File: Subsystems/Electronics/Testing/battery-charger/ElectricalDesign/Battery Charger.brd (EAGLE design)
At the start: 100 x 80 mm, 61 parts, among them J1 USB4515-GF-A_REVA, Q1 CSD16406Q3, Q2 CSD16406Q3, Q3 DMN2008LFU, Q4 DMN2008LFU, Q5 DMN2008LFU, U1 BQ24650, U2 BQ29700, U3 BQ29700, U4 BQ29700

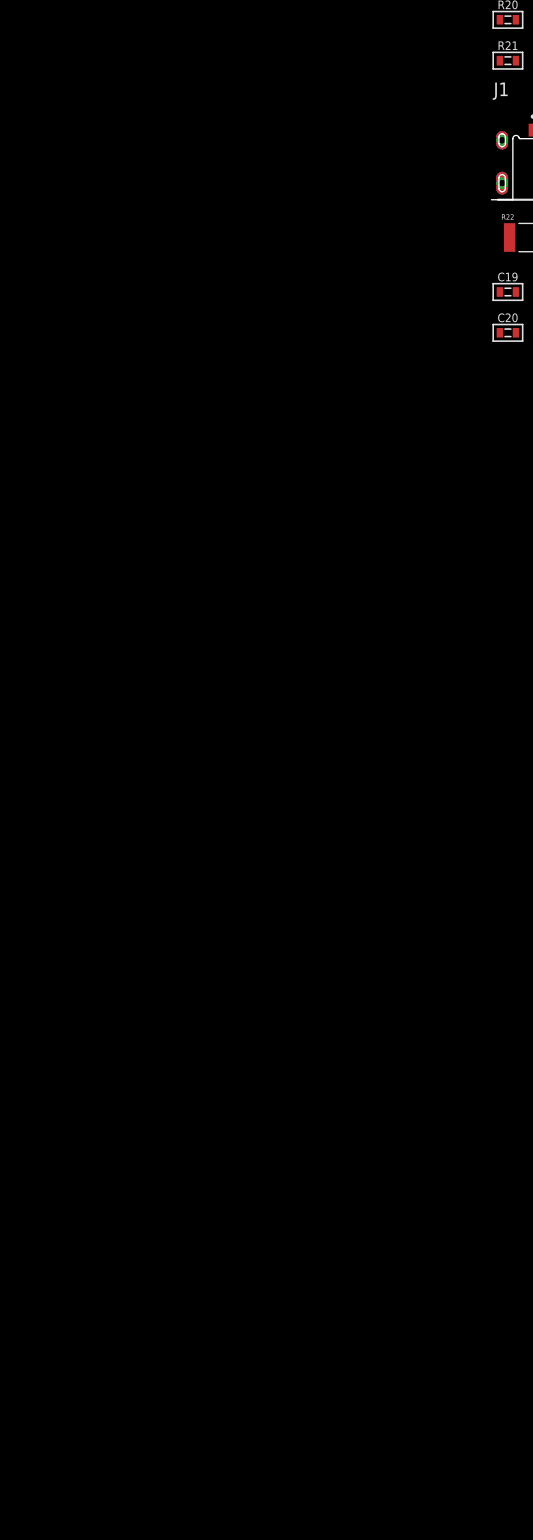
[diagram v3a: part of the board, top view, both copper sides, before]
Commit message: Finished Switching and Battery Protection Circuits
Pages 1-3 are basically finished, while the main components for page 4 have been imported
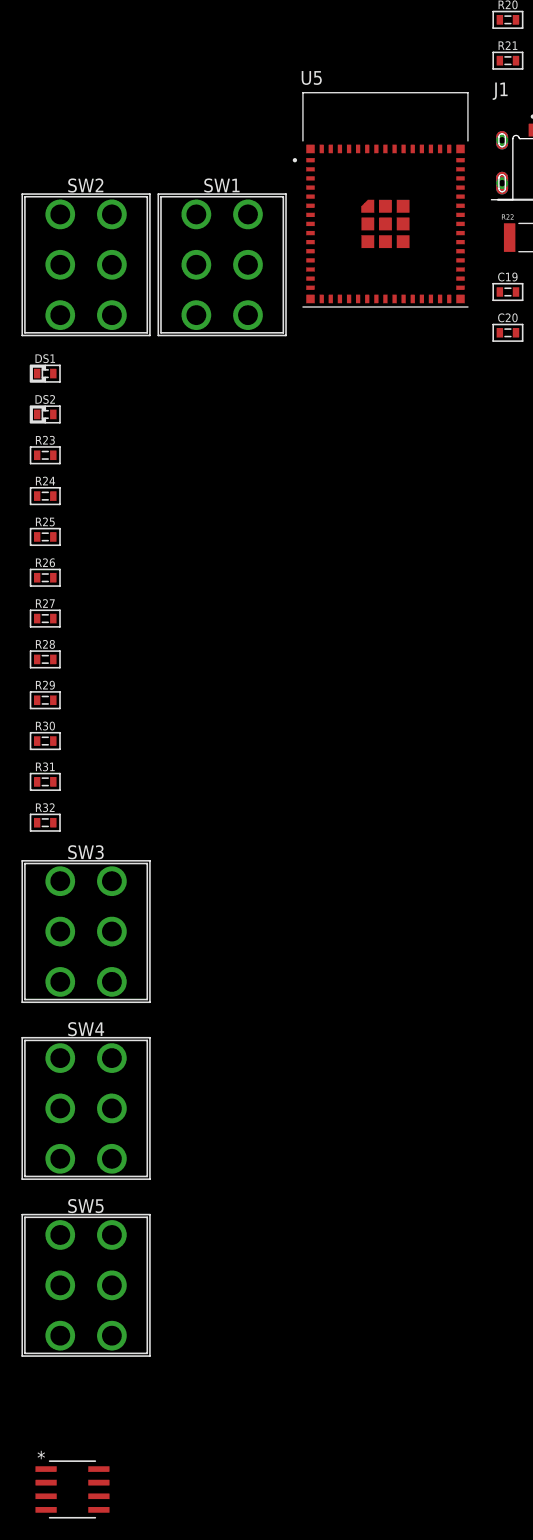
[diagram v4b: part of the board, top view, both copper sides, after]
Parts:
- added DS1: Red, CougsInSpace-LEDs:1608-POL
- added DS2: Green, CougsInSpace-LEDs:1608-POL
- added R23, R24: 10kΩ 0.1%, CougsInSpace-Resistors:1608
- added R25, R28, R30, R32: 442kΩ 1%, CougsInSpace-Resistors:1608
- added R26, R27, R29, R31: 33kΩ 1%, CougsInSpace-Resistors:1608
- added SW1, SW2, SW3, SW4, SW5: (no value), CougsInSpace-Switches:100DP1T1B1M2QE
- added U5: ESP32-S2-MINI-1, ESP32-S2-MINI-1:XCVR_ESP32-S2-MINI-1
- added U7: LT1129IS8-3.3, LT1129IS8-3.3:SO-8_S
- C20: value 1µF 10% -> 10µF 10%
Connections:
- new net 3V3: U5.3
- new net GND: U5.1, U5.2, U5.30, U5.42, U5.43, U5.46, U5.47, U5.48, U5.49, U5.50, U5.51, U5.52, U5.53, U5.54, U5.55, U5.56, U5.57, U5.58, U5.59, U5.60, U5.61, U5.61_1, U5.61_2, U5.61_3, U5.61_4, U5.61_5, U5.61_6, U5.61_7, U5.61_8, U5.62, U5.63, U5.64, U5.65
- new net N$21: U7.1, U7.2
- new net N$33: DS2.A, R24.1
- new net N$34: C19.1, C20.1, R22.1
- new net N$35: R25.1, R26.2
- new net N$36: R27.2, R28.1
- new net N$37: R29.2, R30.1
- new net N$38: R31.2, R32.1
- new net STAT1: D1.4, R26.1
- new net STAT2: DS1.C, U1.3
- new net STAT3: DS2.C, U1.5
- new net STAT4: D3.4, R27.1
- new net STAT5: D4.4, R29.1
- new net STAT6: D5.4, R31.1
- new net SW1: D1.3, SW1.COM-A, SW1.COM-B
- new net SW2: R4.1, R5.2, SW2.COM-A, SW2.COM-B, U1.2
- new net SW3: D3.3, SW3.COM-A, SW3.COM-B
- new net SW4: D4.3, SW4.COM-A, SW4.COM-B
- new net SW5: D5.3, SW5.COM-A, SW5.COM-B
- net 5.0V: now also R23.2, R24.2, R25.2, R28.2, R30.2, R32.2, SW1.1-A, SW1.1-B, SW3.1-A, SW3.1-B, SW4.1-A, SW4.1-B, SW5.1-A, SW5.1-B, U7.8
- net N$11: now also DS1.A, R23.1; no longer R4.1, R5.2, U1.2
- net PGND: now also C19.2, C20.2, SW1.2-A, SW1.2-B, SW2.1-A, SW2.1-B, SW3.2-A, SW3.2-B, SW4.2-A, SW4.2-B, SW5.2-A, SW5.2-B, U7.3, U7.6, U7.7

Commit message: USB to UART IC Added
Page 4 should now be complete with the implementation of a USB to UART program converter. ESP32 has been moved to page 5 and outside of the thermistor connection on the charge controller, this should be the last page
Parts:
- added C25, C26: 4.7µF 10%, CougsInSpace-Capacitors:3216
- added C27, C28, C30, C31: 100nF 10%, CougsInSpace-Capacitors:1608
- added C29: 10µF 10%, CougsInSpace-Capacitors:1608
- added C32: C1206C226K8RACTU, C1206C226K8RACTU:CAPC3216X110N
- added DS3, DS4: Green, CougsInSpace-LEDs:1608-POL
- added J2: (no value), CougsInSpace-Connectors:USB-B-FEMALE
- added Q6, Q7: BC817, BC817:SOT95P230X110-3N
- added R33, R34, R35, R36: 10kΩ 0.1%, CougsInSpace-Resistors:1608
- added U$1: LD1117AS33, LD1117AS33:SOT223
- U5: value ESP32-S2-MINI-1 -> CP2102N-A02-GQFN28; device ESP32-S2-MINI-1:XCVR_ESP32-S2-MINI-1 -> CP2102N-A02-GQFN28:QFN50P500X500X80-29N
- U7: value LT1129IS8-3.3 -> ESP32-S2-MINI-1; device LT1129IS8-3.3:SO-8_S -> ESP32-S2-MINI-1:XCVR_ESP32-S2-MINI-1
- moved U5 221.9 mm to (-133.3, -417.8)
- moved U7 69.5 mm to (-104.1, -395.0)
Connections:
- removed net 3V3: U5.3
- removed net GND: U5.1, U5.2, U5.30, U5.42, U5.43, U5.46, U5.47, U5.48, U5.49, U5.50, U5.51, U5.52, U5.53, U5.54, U5.55, U5.56, U5.57, U5.58, U5.59, U5.60, U5.61, U5.61_1, U5.61_2, U5.61_3, U5.61_4, U5.61_5, U5.61_6, U5.61_7, U5.61_8, U5.62, U5.63, U5.64, U5.65
- new net N$25: J2.3, U5.4
- new net N$31: J2.2, U5.5
- new net N$42: C25.1, C27.1, J2.1, R35.2, R36.2, U5.7, U5.8
- new net N$43: DS4.C, U5.18
- new net N$44: C29.1, C31.1, C32.2, U$1.2, U7.3
- new net N$45: DS3.C, U5.19
- new net N$46: Q6.2, R34.1, U5.24
- new net N$47: Q7.2, R33.1, U5.28
- new net N$48: Q7.1, R34.2
- new net N$49: Q6.1, R33.2
- new net N$50: DS3.A, R35.1
- new net N$51: DS4.A, R36.1
- new net UART-ESP_EN: Q6.3
- new net UART-ESP_IO0: Q7.3
- new net UART_RXD-ESP_TXD: U5.25
- new net UART_TXD-ESP_RXD: U5.26
- net 5.0V: now also C30.1, U$1.3; no longer U7.8
- net N$21: now also C26.1, C28.1, U5.6; no longer U7.1, U7.2
- net PGND: now also C25.2, C26.2, C27.2, C28.2, C29.2, C30.2, C31.2, C32.1, J2.4, J2.SHIELD@1, J2.SHIELD@2, U$1.1, U5.29, U5.3, U7.1, U7.2, U7.30, U7.42, U7.43, U7.46, U7.47, U7.48, U7.49, U7.50, U7.51, U7.52, U7.53, U7.54, U7.55, U7.56, U7.57, U7.58, U7.59, U7.60, U7.61, U7.61_1, U7.61_2, U7.61_3, U7.61_4, U7.61_5, U7.61_6, U7.61_7, U7.61_8, U7.62, U7.63, U7.64, U7.65; no longer U7.3, U7.6, U7.7
- net STAT1: now also U7.5
- net STAT2: now also U7.6
- net STAT3: now also U7.7
- net STAT4: now also U7.8
- net STAT5: now also U7.9
- net STAT6: now also U7.10

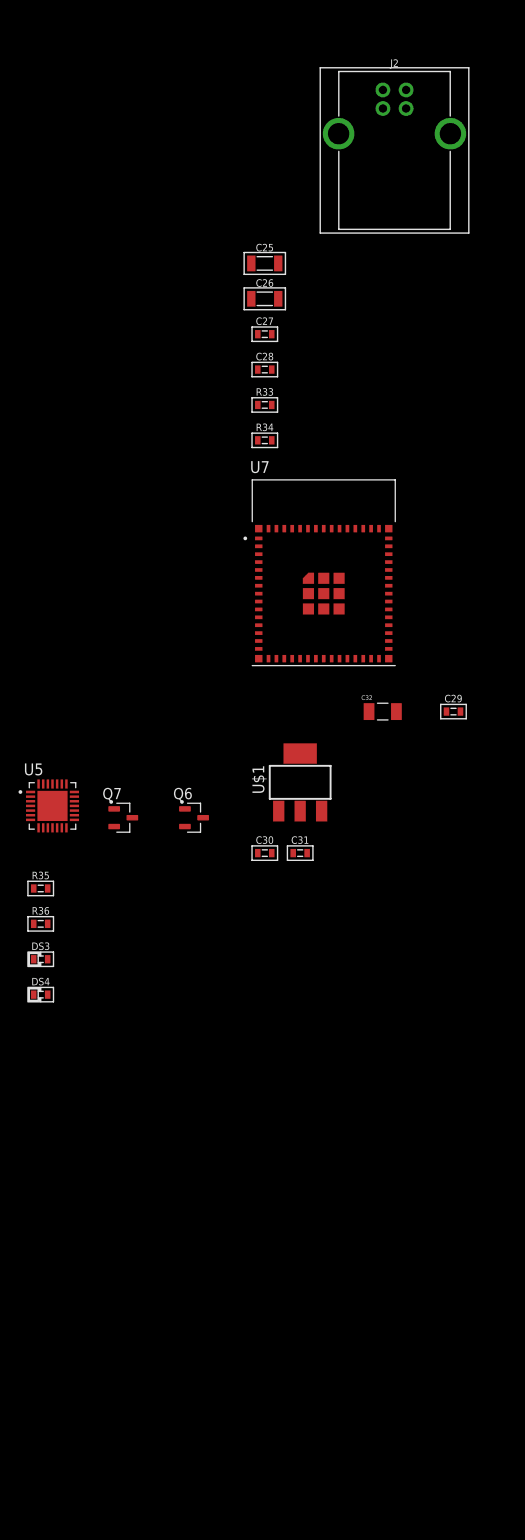
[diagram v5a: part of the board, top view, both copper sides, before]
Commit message: Finished Battery Charger V1
Will add programmable RGB LEDS at some point, and may update at a later date with an LED display, but otherwise this can be considered the base design for the over-engineered battery charger
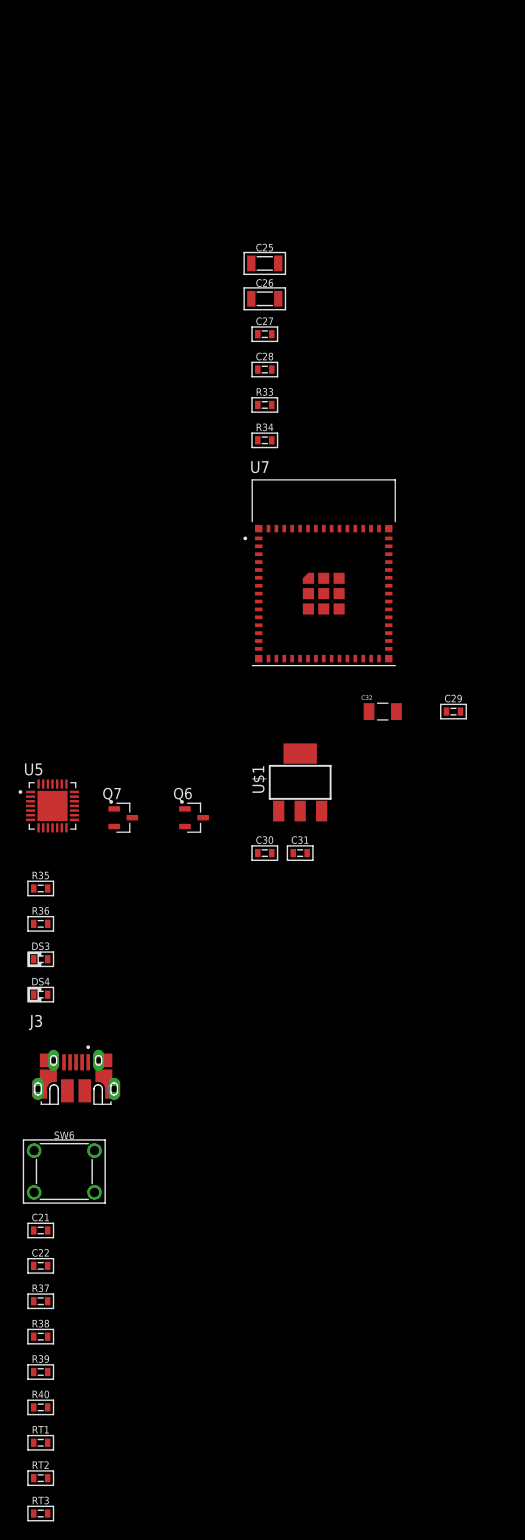
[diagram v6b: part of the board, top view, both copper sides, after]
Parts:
- removed J2: (no value), CougsInSpace-Connectors:USB-B-FEMALE
- added C21, C22: 100nF 10%, CougsInSpace-Capacitors:1608
- added J3: 10103592-0001LF, 10103592-0001LF:AMPHENOL_10103592-0001LF
- added R37, R38, R39, R40: 10kΩ 0.1%, CougsInSpace-Resistors:1608
- added RT1, RT2, RT3: 10kΩ 5%, CougsInSpace-Resistors:1608
- added SW6: [Override], CougsInSpace-Switches:THT-6060
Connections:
- removed net N$44: C29.1, C31.1, C32.2, U$1.2, U7.3
- new net 3.3V: C29.1, C31.1, C32.2, R37.2, R38.2, R39.2, R40.2, U$1.2, U7.3
- new net TEMP1: R38.1, RT1.2, U7.11
- new net TEMP2: R39.1, RT2.2, U7.12
- new net TEMP3: R40.1, RT3.2, U7.13
- new net TS-ESP: U1.4, U7.14
- net N$25: now also J3.3; no longer J2.3
- net N$31: now also J3.2; no longer J2.2
- net N$42: now also J3.1; no longer J2.1
- net PGND: now also C21.1, C22.2, J3.5, J3.S1, J3.S2, J3.S3, J3.S4, J3.S5, J3.S6, RT1.1, RT2.1, RT3.1, SW6.1, SW6.2; no longer J2.4, J2.SHIELD@1, J2.SHIELD@2
- net UART-ESP_EN: now also C21.2, C22.1, R37.1, SW6.3, SW6.4, U7.45
- net UART-ESP_IO0: now also U7.4
- net UART_RXD-ESP_TXD: now also U7.39
- net UART_TXD-ESP_RXD: now also U7.40

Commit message: Added RGB LEDs
Final touches for V1 including CAD notes and addressable LEDs have been added
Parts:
- added C23, C24, C33: 100nF 10%, CougsInSpace-Capacitors:1608
- added D6, D7, D8: SK6812, SK6812:LED_SK6812
- added JP1: (no value), pinhead:1X07
- added JP2: (no value), pinhead:1X16
- added R41: 330Ω 1%, CougsInSpace-Resistors:1608
- DS1: value Red -> Yellow
- moved DS1 277.5 mm to (-134.6, -497.8)
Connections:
- new net LEDS: R41.1, U7.15
- new net N$44: JP2.1, U7.23
- new net N$52: JP2.2, U7.24
- new net N$53: JP2.3, U7.25
- new net N$54: JP2.4, U7.26
- new net N$55: JP2.5, U7.28
- new net N$56: JP2.6, U7.29
- new net N$57: JP2.7, U7.31
- new net N$58: JP2.8, U7.32
- new net N$59: JP2.9, U7.33
- new net N$60: JP2.10, U7.34
- new net N$61: JP2.11, U7.35
- new net N$62: JP2.12, U7.36
- new net N$63: JP2.13, U7.37
- new net N$64: JP2.14, U7.38
- new net N$65: JP2.15, U7.41
- new net N$66: JP2.16, U7.44
- new net N$67: D7.2, D8.4
- new net N$68: JP1.7, U7.16
- new net N$69: JP1.6, U7.17
- new net N$70: JP1.5, U7.18
- new net N$71: JP1.4, U7.19
- new net N$72: JP1.3, U7.20
- new net N$73: JP1.2, U7.21
- new net N$74: JP1.1, U7.22
- new net N$76: D6.2, D7.4
- new net N$77: D6.4, R41.2
- net 5.0V: now also C23.1, C24.1, C33.1, D6.1, D7.1, D8.1
- net PGND: now also C23.2, C24.2, C33.2, D6.3, D7.3, D8.3

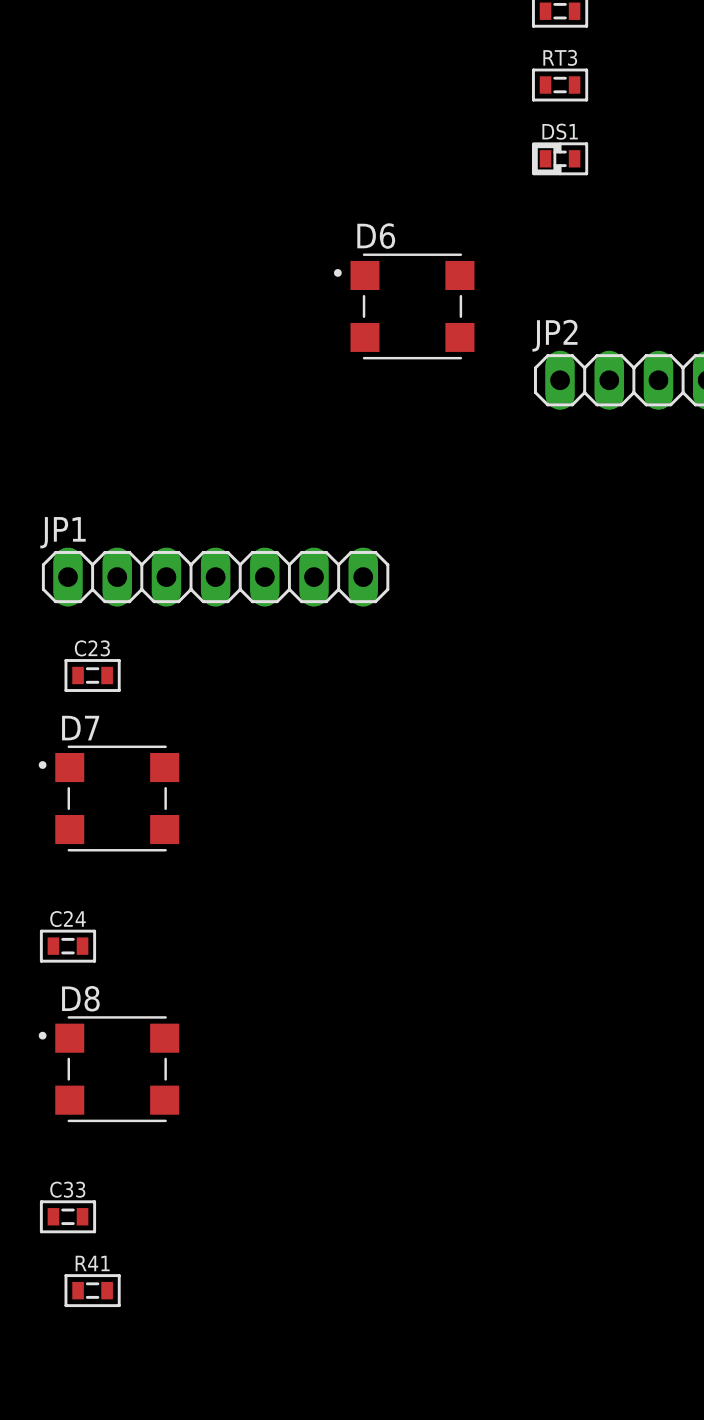
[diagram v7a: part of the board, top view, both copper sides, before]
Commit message: Tidied Up Schematic
Named all major nets, formatted in and out markings to match other CIS schematics, and adjusted LED colors to match convention.
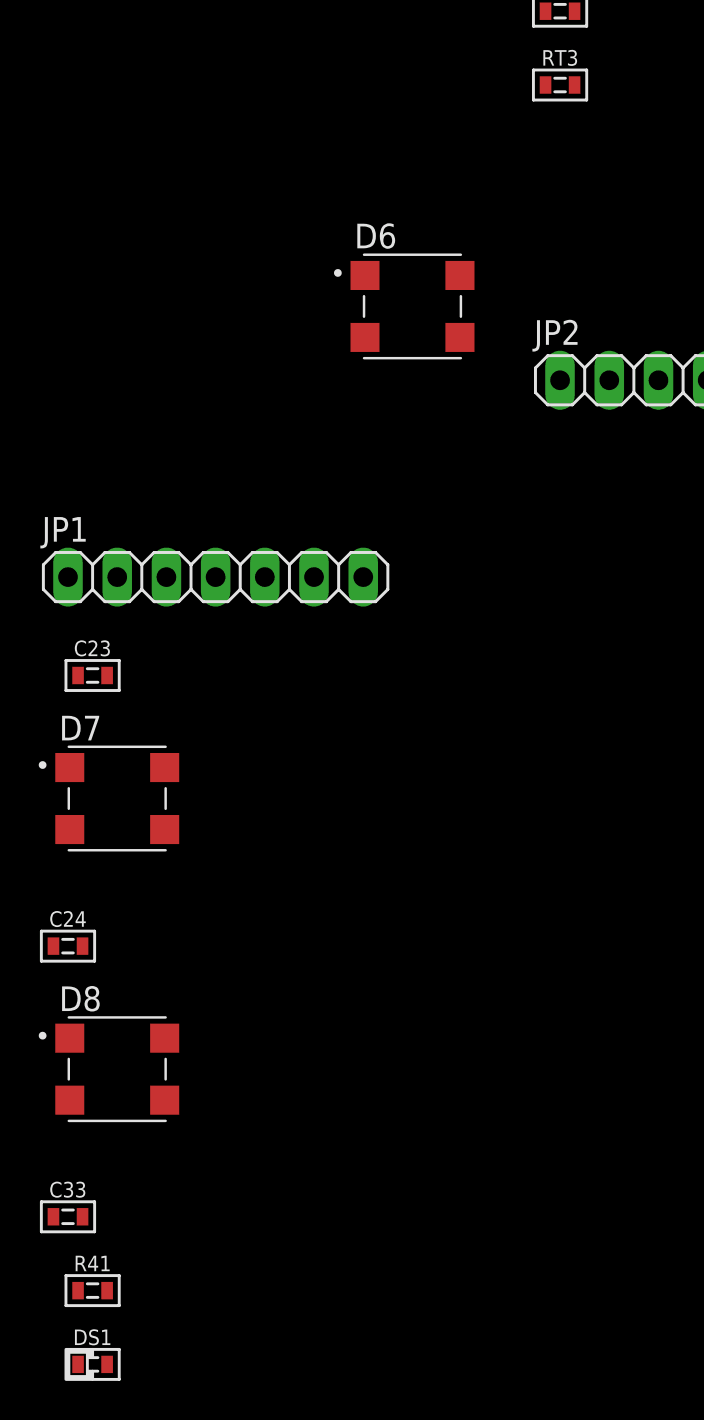
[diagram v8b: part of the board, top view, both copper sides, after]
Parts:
- DS1: value Yellow -> Blue
- moved DS1 66.7 mm to (-158.8, -560.1)
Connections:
- net CHARGER-SWITCHING renamed CHARGER
- net N$1 renamed BQ24650_VREF
- net N$10 renamed BQ24650_HIGHDV
- net N$12 renamed BQ24650_LODRV
- net N$13 renamed BQ297001_V-
- net N$14 renamed BQ297002_V-
- net N$16 renamed BQ297001_COUT
- net N$17 renamed BQ297001_DOUT
- net N$18 renamed BQ297001_VSS
- net N$19 renamed BQ297002_COUT
- net N$2 renamed D1_OUT
- net N$20 renamed BQ297001_BAT
- net N$21 renamed CP2102N_VDD
- net N$22 renamed BQ297002_DOUT
- net N$23 renamed BQ297002_VSS
- net N$24 renamed BQ297002_BAT
- net N$25 renamed D+
- net N$26 renamed BQ297003_V-
- net N$27 renamed BQ297003_COUT
- net N$28 renamed BQ297003_DOUT
- net N$29 renamed BQ297003_VSS
- net N$3 renamed BQ24650_REGN
- net N$30 renamed BQ297003_BAT
- net N$31 renamed D-
- net N$39 renamed D3_OUT
- net N$4 renamed BQ24650_PH
- net N$40 renamed D4_OUT
- net N$41 renamed D5_OUT
- net N$42 renamed USB_VDD
- net N$43 renamed CP2102N_RXT
- net N$44 renamed ESP32_IO19
- net N$45 renamed CP2102N_TXT
- net N$46 renamed CP2102N_RTS
- net N$47 renamed CP2102N_DTR
- net N$5 renamed BQ24650_BTST
- net N$52 renamed ESP32_IO20
- net N$53 renamed ESP32_IO21
- net N$54 renamed ESP32_IO26
- net N$55 renamed ESP32_IO33
- net N$56 renamed ESP32_IO34
- net N$57 renamed ESP32_IO35
- net N$58 renamed ESP32_IO36
- net N$59 renamed ESP32_IO37
- net N$6 renamed BQ24650_VCC
- net N$60 renamed ESP32_IO38
- net N$61 renamed ESP32_IO39
- net N$62 renamed ESP32_IO40
- net N$63 renamed ESP32_IO41
- net N$64 renamed ESP32_IO42
- net N$65 renamed ESP32_IO45
- net N$66 renamed ESP32_IO46
- net N$67 renamed LED3_DIN
- net N$68 renamed ESP32_IO12
- net N$69 renamed ESP32_IO13
- net N$7 renamed BQ24650_SR_P
- net N$70 renamed ESP32_IO14
- net N$71 renamed ESP32_IO15
- net N$72 renamed ESP32_IO16
- net N$73 renamed ESP32_IO17
- net N$74 renamed ESP32_IO18
- net N$76 renamed LED2_DIN
- net N$77 renamed LED1_DIN
- net N$9 renamed BQ24650_VFB
